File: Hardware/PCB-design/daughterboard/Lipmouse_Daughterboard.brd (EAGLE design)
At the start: 35 x 35 mm, 9 parts

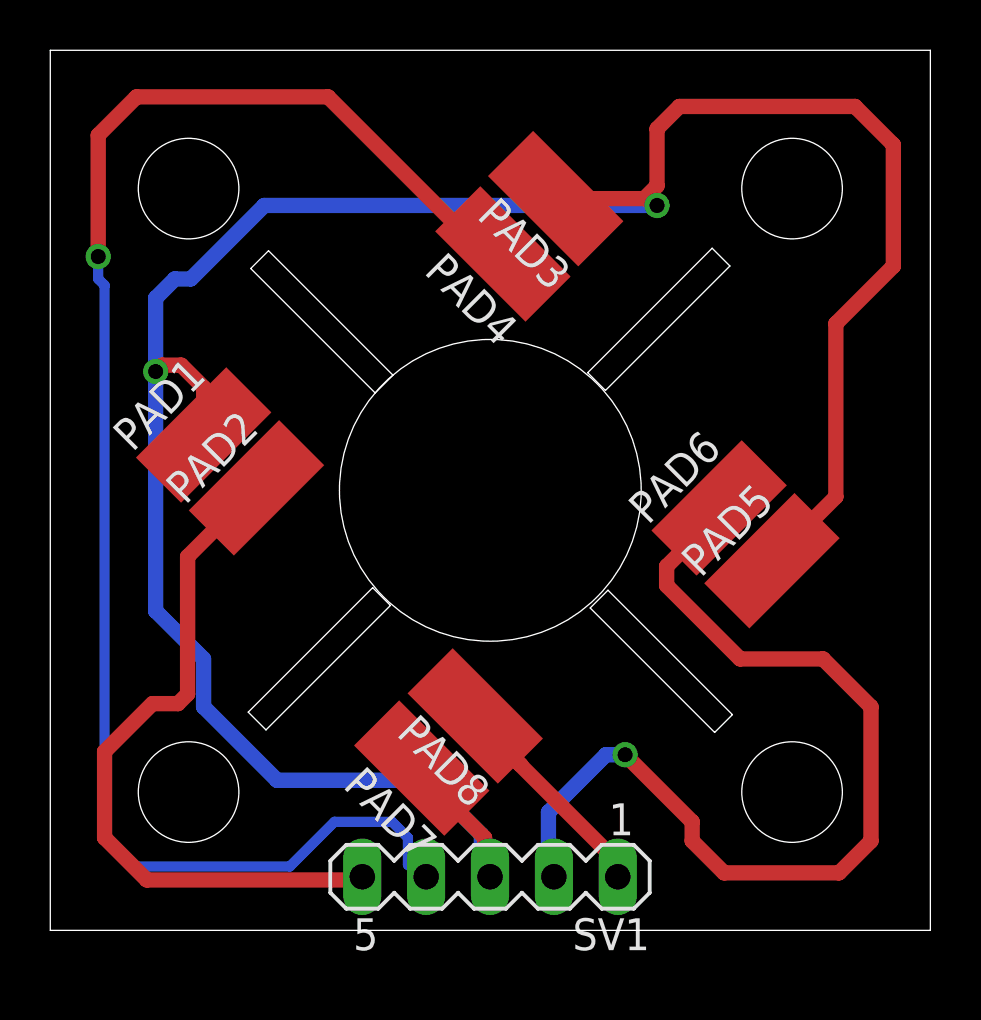
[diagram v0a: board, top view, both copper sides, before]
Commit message: Update daughterboard: Reduce size for case/mainboard v2 Cut corners, to ensure easy assembly, even with glue stains in the case
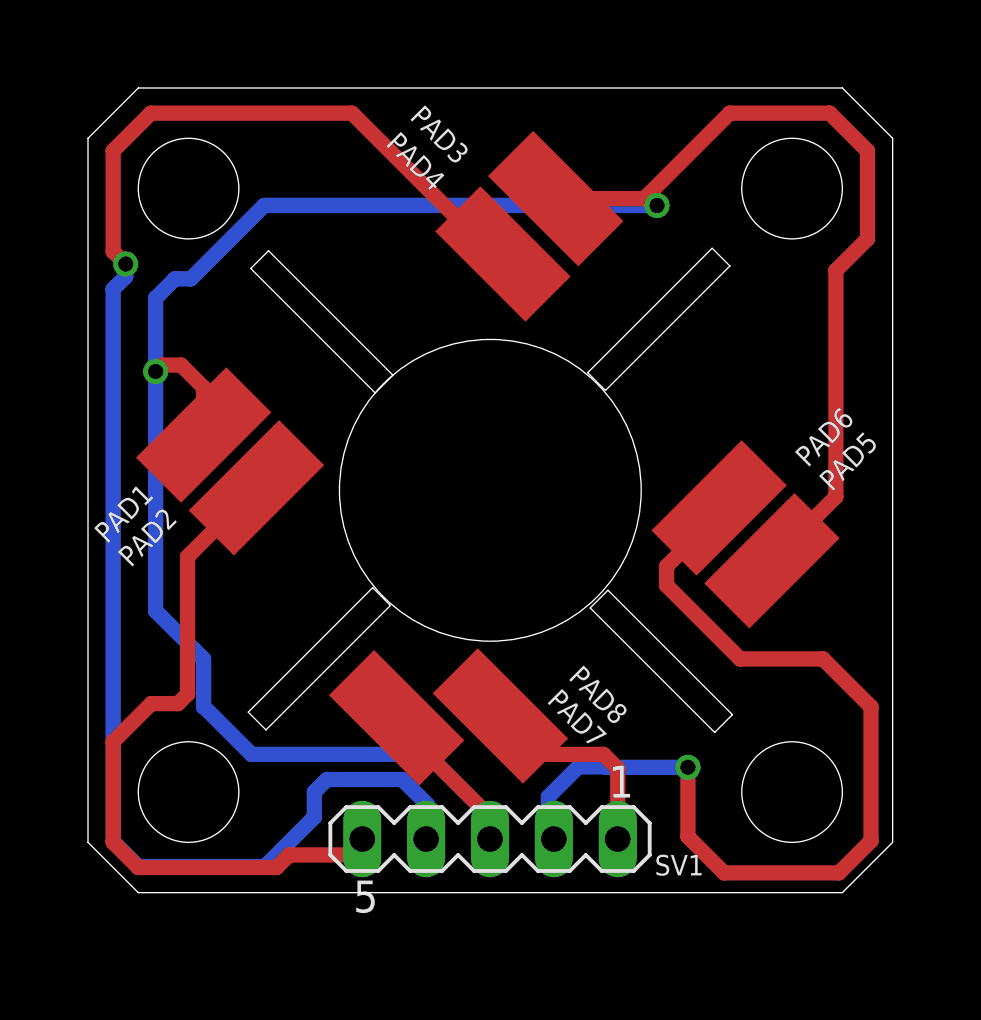
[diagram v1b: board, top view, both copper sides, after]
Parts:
- moved PAD7 2.24 mm to (13.8, 8.45)
- moved SV1 1.50 mm to (17.5, 3.63)
- moved PAD8 1.00 mm to (17.9, 8.53)
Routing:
- net 3V3: track 100.8 -> 96.2 mm
- net N$23: track 11.5 -> 12.9 mm
- net N$22: track 38.9 -> 38.4 mm
- net N$21: track 62.8 -> 63.3 mm
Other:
- board size 35 x 35 mm -> 32 x 32 mm
